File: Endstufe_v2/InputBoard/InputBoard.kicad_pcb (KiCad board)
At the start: 4 copper layers, 85 x 50 mm, 65 parts, among them J1 ST-0322D00-071-1A2H, J11 DNP, J2 ST-0322D00-071-1A2H, J3 ST-0322D00-071-1A2H, J4 ST-0322D00-071-1A2H, J5 B4B-XH-2_(LF)(SN), J6 B4B-XH-2_(LF)(SN), J7 B4B-XH-2_(LF)(SN), J8 Conn_01x02_Pin, J9 B4B-XH-2_(LF)(SN), U1 PCM1865DBTR, U2 PCM9211PTR, U4 ZPLR135_T8, U5 ZPLR135_T8, U6 ZPLR135_T8, U7 ZPLR135_T8, Y1 24.576Mhz, Y2 24.576Mhz

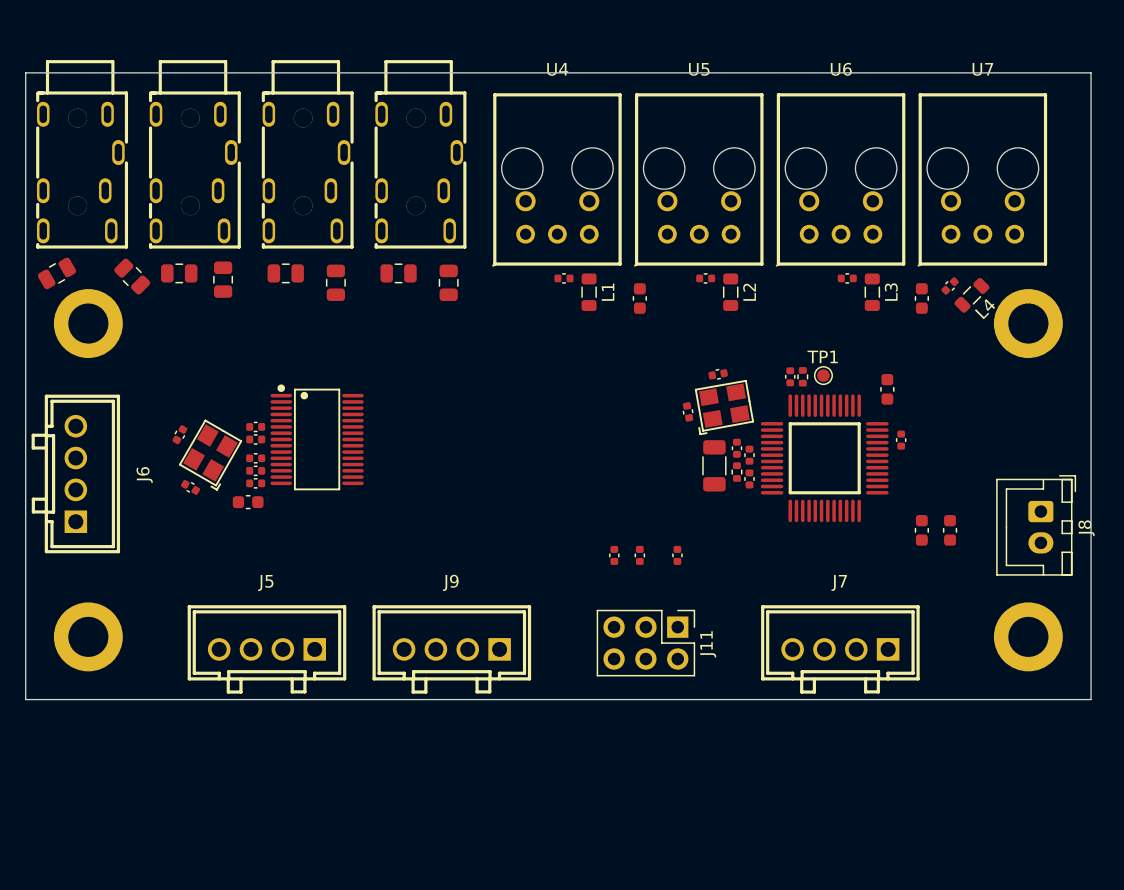
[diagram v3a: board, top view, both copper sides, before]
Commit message: Finish layout of control and input board for now
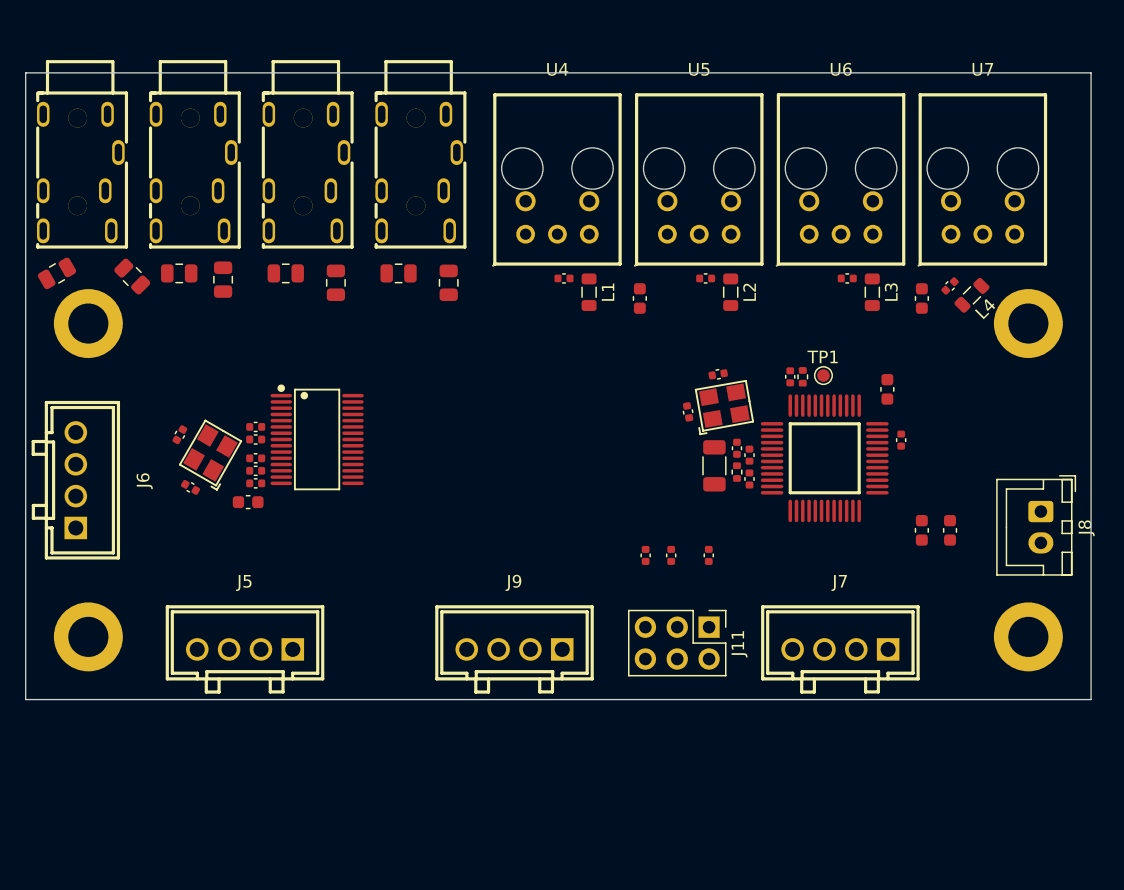
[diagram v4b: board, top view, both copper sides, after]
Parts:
- moved J9 5.00 mm to (109.0, 116.0)
- moved J11 2.50 mm to (124.5, 114.2)
- moved R2 2.50 mm to (119.5, 108.5)
- moved R3 2.50 mm to (121.5, 108.5)
- moved R5 2.50 mm to (124.5, 108.5)
- moved J5 1.75 mm to (87.5, 116.0)
- moved J6 0.50 mm to (74.0, 102.5)
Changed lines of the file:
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@@
 	(footprint "Connector_PinHeader_2.54mm:PinHeader_2x03_P2.54mm_Vertical"
 		(layer "F.Cu")
-		(at 122.025 114.225 -90)
+		(at 124.525 114.225 -90)
 		(descr "Through hole straight pin header, 2x03, 2.54mm pitch, double rows")
 		(tags "Through hole pin header THT 2x03 2.54mm double row")
@@
 		)
 		(fp_text user "${REFERENCE}"
-			(at 1.27 2.54 360)
+			(at 1.27 2.54 0)
 			(layer "F.Fab")
 			(effects
@@
 	(footprint "Endstufe:C_0402_1005Metric"
 		(layer "F.Cu")
-		(at 119 108.5 90)
+		(at 121.5 108.5 90)
 		(descr "Capacitor SMD 0402 (1005 Metric), square (rectangular) end terminal, IPC_7351 nominal, (Body size source: IPC-SM-782 page 76, https://www.pcb-3d.com/wordpress/wp-content/uploads/ipc-sm-782a_amendment_1_and_2.pdf), generated with kicad-footprint-generator")
 		(tags "capacitor")
@@
 			(end -5 3.694996)
 			(stroke
-				(width 0.254001)
+				(width 0.254)
 				(type solid)
 			)
@@
 			(end 5 -9.805029)
 			(stroke
-				(width 0.254001)
+				(width 0.254)
 				(type solid)
 			)
@@
 			(end 5 3.694996)
 			(stroke
-				(width 0.254001)
+				(width 0.254)
 				(type solid)
 			)
@@
 			(end 5 3.694996)
 			(stroke
-				(width 0.254001)
+				(width 0.254)
 				(type solid)
 			)
@@
 	(footprint "Endstufe:CONN-TH_B4B-XH-2-LF-SN"
 		(layer "F.Cu")
-		(at 89.25 116)
+		(at 87.5 116)
 		(descr "CONN-TH_B4B-XH-2-LF-SN footprint")
 		(tags "CONN-TH_B4B-XH-2-LF-SN footprint C157999")
@@
 	)
 	(footprint "Endstufe:CONN-TH_B4B-XH-2-LF-SN"
+		(locked yes)
 		(layer "F.Cu")
-		(at 74 102 -90)
+		(at 74 102.5 -90)
 		(descr "CONN-TH_B4B-XH-2-LF-SN footprint")
 		(tags "CONN-TH_B4B-XH-2-LF-SN footprint C157999")
@@
 	(footprint "Endstufe:C_0402_1005Metric"
 		(layer "F.Cu")
-		(at 122 108.5 90)
+		(at 124.5 108.5 90)
 		(descr "Capacitor SMD 0402 (1005 Metric), square (rectangular) end terminal, IPC_7351 nominal, (Body size source: IPC-SM-782 page 76, https://www.pcb-3d.com/wordpress/wp-content/uploads/ipc-sm-782a_amendment_1_and_2.pdf), generated with kicad-footprint-generator")
 		(tags "capacitor")
@@
 			(end -5 3.694996)
 			(stroke
-				(width 0.254001)
+				(width 0.254)
 				(type solid)
 			)
@@
 			(end 5 -9.805029)
 			(stroke
-				(width 0.254001)
+				(width 0.254)
 				(type solid)
 			)
@@
 			(end 5 3.694996)
 			(stroke
-				(width 0.254001)
+				(width 0.254)
 				(type solid)
 			)
@@
 			(end 5 3.694996)
 			(stroke
-				(width 0.254001)
+				(width 0.254)
 				(type solid)
 			)
@@
 			(end -5 3.694996)
 			(stroke
-				(width 0.254001)
+				(width 0.254)
 				(type solid)
 			)
@@
 			(end 5 -9.805029)
 			(stroke
-				(width 0.254001)
+				(width 0.254)
 				(type solid)
 			)
@@
 			(end 5 3.694996)
 			(stroke
-				(width 0.254001)
+				(width 0.254)
 				(type solid)
 			)
@@
 			(end 5 3.694996)
 			(stroke
-				(width 0.254001)
+				(width 0.254)
 				(type solid)
 			)
@@
 		(locked yes)
 		(layer "F.Cu")
-		(at 104 116)
+		(at 109 116)
 		(descr "CONN-TH_B4B-XH-2-LF-SN footprint")
 		(tags "CONN-TH_B4B-XH-2-LF-SN footprint C157999")
@@
 	(footprint "Endstufe:C_0402_1005Metric"
 		(layer "F.Cu")
-		(at 116.965 108.5 90)
+		(at 119.465 108.5 90)
 		(descr "Capacitor SMD 0402 (1005 Metric), square (rectangular) end terminal, IPC_7351 nominal, (Body size source: IPC-SM-782 page 76, https://www.pcb-3d.com/wordpress/wp-content/uploads/ipc-sm-782a_amendment_1_and_2.pdf), generated with kicad-footprint-generator")
 		(tags "capacitor")
@@
 			(end -5 3.694996)
 			(stroke
-				(width 0.254001)
+				(width 0.254)
 				(type solid)
 			)
@@
 			(end 5 -9.805029)
 			(stroke
-				(width 0.254001)
+				(width 0.254)
 				(type solid)
 			)
@@
 			(end 5 3.694996)
 			(stroke
-				(width 0.254001)
+				(width 0.254)
 				(type solid)
 			)
@@
 			(end 5 3.694996)
 			(stroke
-				(width 0.254001)
+				(width 0.254)
 				(type solid)
 			)

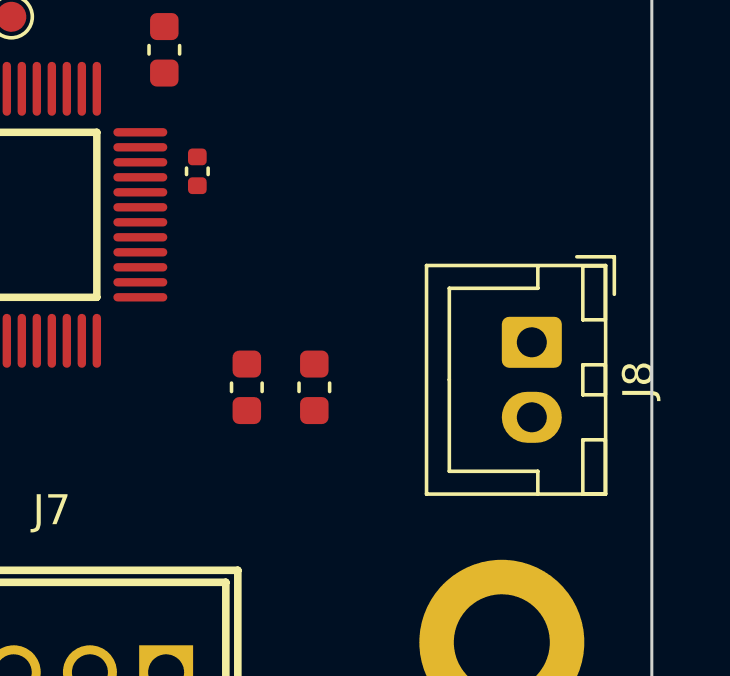
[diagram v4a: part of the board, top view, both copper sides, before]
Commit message: Add forgotten 3V3 outputs to control board
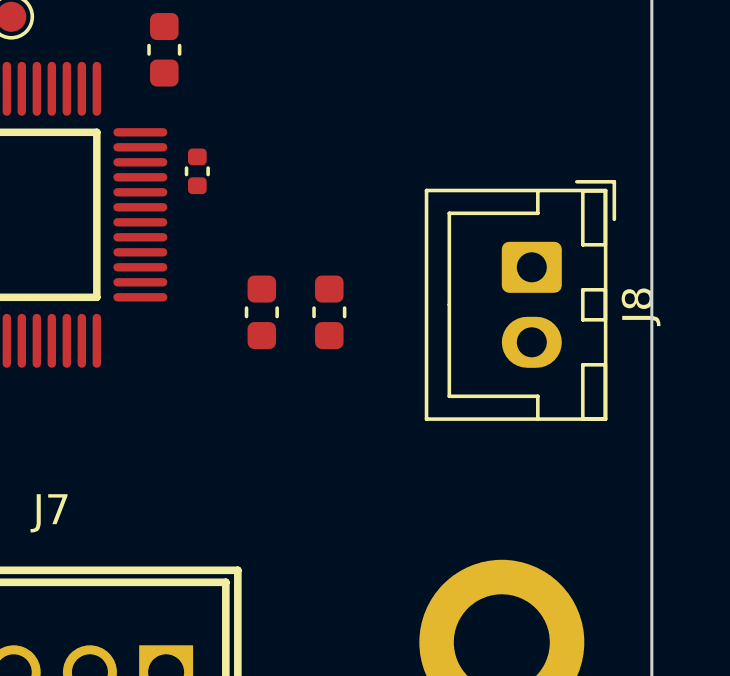
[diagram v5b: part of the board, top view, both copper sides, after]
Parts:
- moved C28 2.55 mm to (142.0, 104.0)
- moved C29 2.55 mm to (144.2, 104.0)
- moved J8 2.50 mm to (151.0, 102.5)
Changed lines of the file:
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@@
 	)
 	(footprint "Connector_JST:JST_XH_B2B-XH-A_1x02_P2.50mm_Vertical"
-		(locked yes)
 		(layer "F.Cu")
-		(at 151 105 -90)
+		(at 151 102.5 -90)
 		(descr "JST XH series connector, B2B-XH-A (http://www.jst-mfg.com/product/pdf/eng/eXH.pdf), generated with kicad-footprint-generator")
 		(tags "connector JST XH vertical")
@@
 	(footprint "Endstufe:C_0603_1608Metric"
 		(layer "F.Cu")
-		(at 143.75 106.5 90)
+		(at 144.25 104 90)
 		(descr "Capacitor SMD 0603 (1608 Metric), square (rectangular) end terminal, IPC_7351 nominal, (Body size source: IPC-SM-782 page 76, https://www.pcb-3d.com/wordpress/wp-content/uploads/ipc-sm-782a_amendment_1_and_2.pdf), generated with kicad-footprint-generator")
 		(tags "capacitor")
@@
 	(footprint "Endstufe:C_0603_1608Metric"
 		(layer "F.Cu")
-		(at 141.5 106.5 90)
+		(at 142 104 90)
 		(descr "Capacitor SMD 0603 (1608 Metric), square (rectangular) end terminal, IPC_7351 nominal, (Body size source: IPC-SM-782 page 76, https://www.pcb-3d.com/wordpress/wp-content/uploads/ipc-sm-782a_amendment_1_and_2.pdf), generated with kicad-footprint-generator")
 		(tags "capacitor")

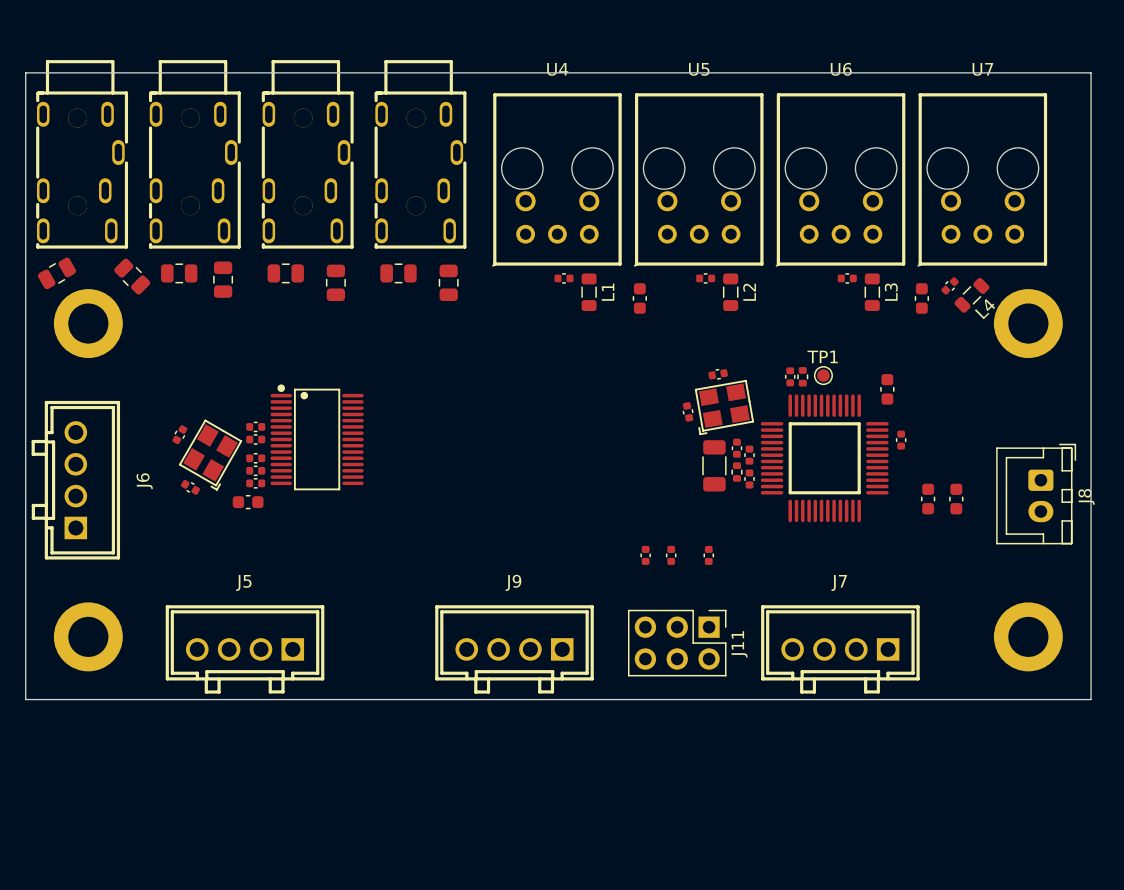
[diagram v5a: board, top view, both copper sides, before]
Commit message: Route input board
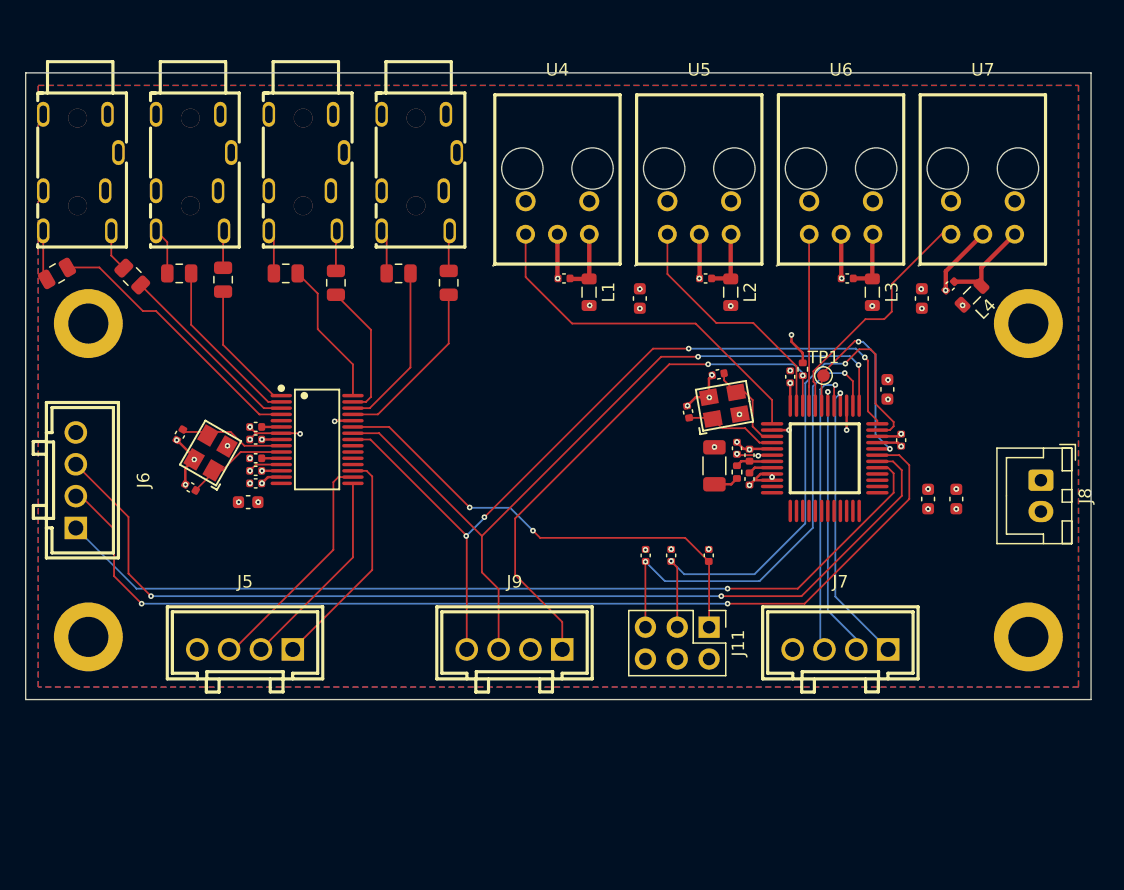
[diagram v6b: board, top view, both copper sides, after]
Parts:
- moved R1 0.60 mm to (132.0, 93.7)
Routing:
- net /PCM9211/BCK: track 0.00 -> 81.3 mm, vias 0 -> 2
- net /PCM9211/LRCK: track 0.00 -> 80.5 mm, vias 0 -> 2
- net /PCM9211/DOUT: track 0.00 -> 73.5 mm, vias 0 -> 1
- net /PCM1865/SDA: track 0.00 -> 65.4 mm, vias 0 -> 4
- net /PCM1865/SCL: track 0.00 -> 62.9 mm, vias 0 -> 2
- net GND: track 0.00 -> 46.2 mm, vias 0 -> 37
- net /PCM9211/ADR0: track 0.00 -> 44.3 mm, vias 0 -> 2
- net /PCM9211/RST: track 0.00 -> 43.0 mm, vias 0 -> 2
- net /PCM9211/ADR1: track 0.00 -> 38.1 mm, vias 0 -> 2
- net /PCM1865/ADR0: track 0.00 -> 38.1 mm, vias 0 -> 2
- net /PCM9211/SPDIF0: track 0.00 -> 29.0 mm
- net /PCM9211/LRCKI: track 0.00 -> 24.0 mm, vias 0 -> 1
- net /PCM9211/DIN: track 0.00 -> 23.4 mm, vias 0 -> 1
- net /PCM9211/BCKI: track 0.00 -> 22.6 mm, vias 0 -> 1
- net /PCM1865/VINR1: track 0.00 -> 21.9 mm
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- added copper zone on B.Cu, net +3V3
- added copper zone on F.Cu, net GND
- added copper zone on In1.Cu, net GND
- added copper zone on In2.Cu, net GND

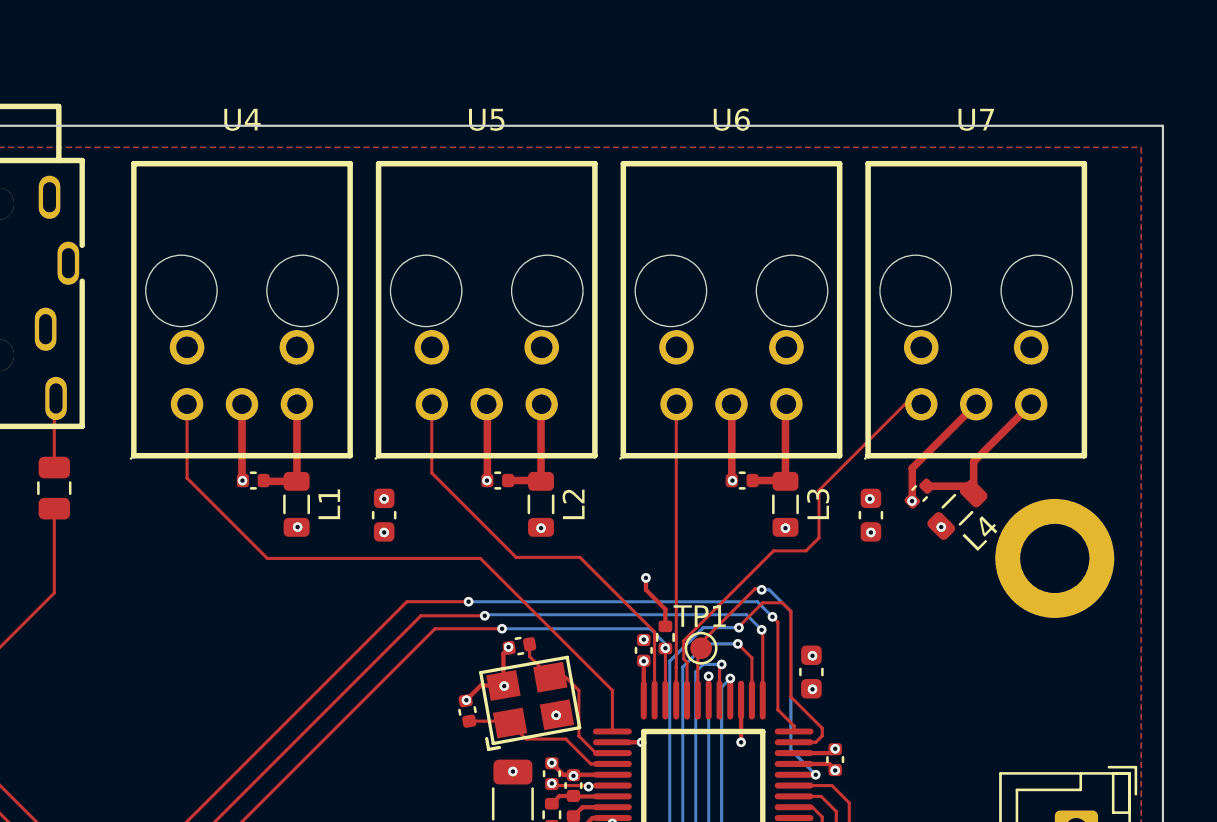
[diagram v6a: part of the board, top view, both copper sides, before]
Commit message: Move up SPDIF connectors
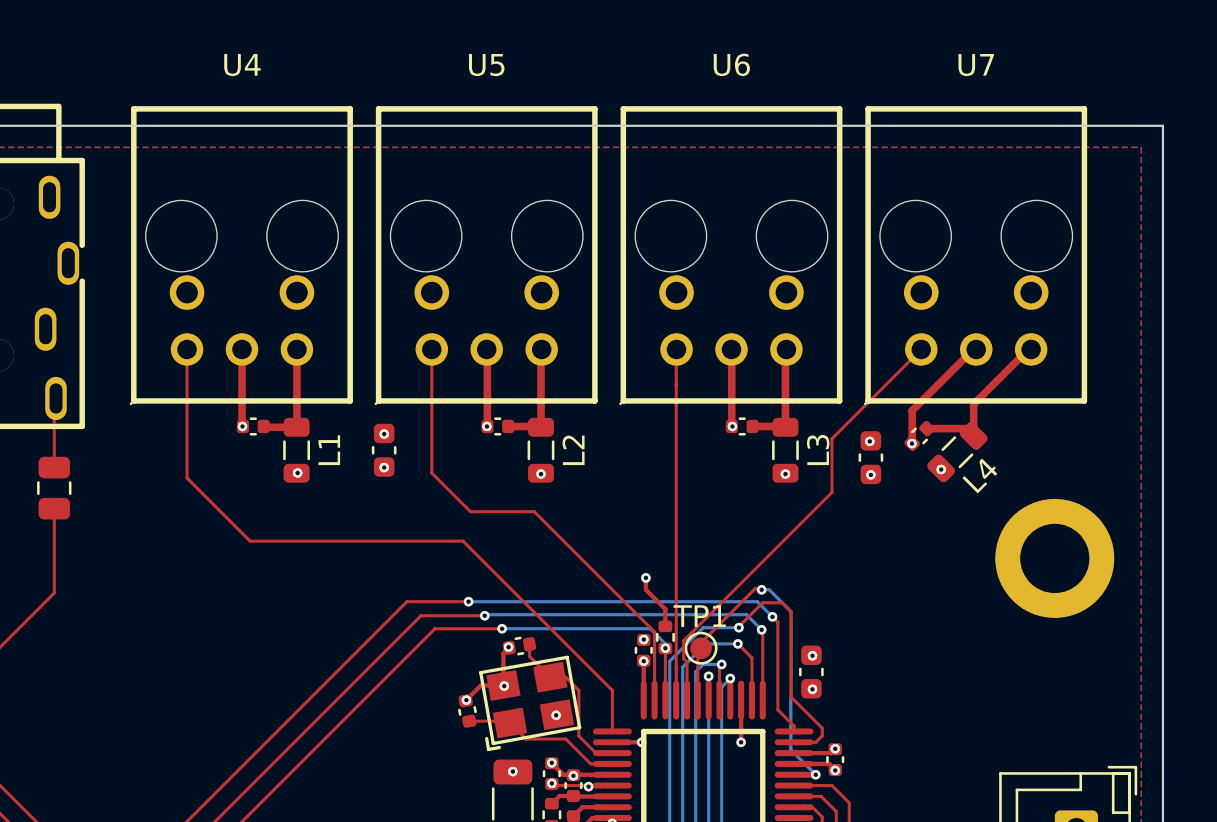
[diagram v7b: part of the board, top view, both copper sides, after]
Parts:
- moved C30 3.00 mm to (119.0, 85.0)
- moved C18 2.66 mm to (143.7, 84.3)
- moved C31 2.66 mm to (141.5, 85.3)
- moved L4 2.66 mm to (145.5, 85.1)
- moved U4 2.53 mm to (112.4, 79.0)
- moved U5 2.53 mm to (123.7, 79.0)
- moved U6 2.53 mm to (135.1, 79.0)
- moved U7 2.53 mm to (146.4, 79.0)
- moved C22 2.50 mm to (113.0, 83.9)
- moved C23 2.50 mm to (124.2, 83.9)
- moved C24 2.50 mm to (135.6, 83.9)
- moved L1 2.50 mm to (115.0, 85.0)
- moved L2 2.50 mm to (126.2, 85.0)
- moved L3 2.50 mm to (137.6, 85.0)
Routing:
- net /PCM9211/SPDIF2: track 13.7 -> 16.3 mm
- net /PCM9211/SPDIF0: track 29.0 -> 31.6 mm
- net /PCM9211/SPDIF1: track 19.7 -> 22.2 mm
- net /PCM9211/SPDIF3: track 19.6 -> 20.8 mm
